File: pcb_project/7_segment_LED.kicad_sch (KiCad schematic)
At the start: 1 part, among them U5 MAX7221xWG

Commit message: LED & FPGA_Started
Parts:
- added C24: 10µF electrolytic, symbol Device:C
- added C25: 0.1µF ceramic, symbol Device:C
- added R40: 18KOhm, symbol Device:R
- added U6: COM-11405, COM-11405_SPK, symbol 11405_ATA8041:COM-11405
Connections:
- net LED_MOSI: now reaches U5.1 (DIN)
- net at U5.11 (DIG_1): now also U6.9 (DIG2)
- net LED_CS: now reaches U5.12 (~{CS})
- net LED_CLK: now reaches U5.13 (CLK)
- net SEGA (11): now reaches U5.14 (SEG_A)
- net SEGA (11): now also U6.11 (A)
- net SEGF (10): now reaches U5.15 (SEG_F)
- net SEGF (10): now also U6.10 (F)
- net SEGB (7): now reaches U5.16 (SEG_B)
- net SEGB (7): now also U6.7 (B)
- net SEGG (5): now reaches U5.17 (SEG_G)
- net SEGG (5): now also U6.5 (G)
- net at U5.18 (ISET): now also R40.2
- net +5V: now reaches U5.19 (V+)
- net +5V: now also C24.1, C25.1, R40.1
- net at U5.2 (DIG_0): now also U6.12 (Dig1)
- net SEGC (4): now reaches U5.20 (SEG_C)
- net SEGC (4): now also U6.4 (C)
- net SEGE (1): now reaches U5.21 (SEG_E)
- net SEGE (1): now also U6.1 (E)
- net at U5.22 (SEG_DP): now also U6.3 (DP)
- net SEGD(2): now reaches U5.23 (SEG_D)
- net SEGD(2): now also U6.2 (D)
- net LED_MISO: now reaches U5.24 (DOUT)
- net GND: now reaches U5.4 (GND), U5.9 (GND)
- net GND: now also C24.2, C25.2
- net at U5.6 (DIG_2): now also U6.8 (DIG3)
- net at U5.7 (DIG_3): now also U6.6 (DIG4)
- no-connect marks 0 -> 4

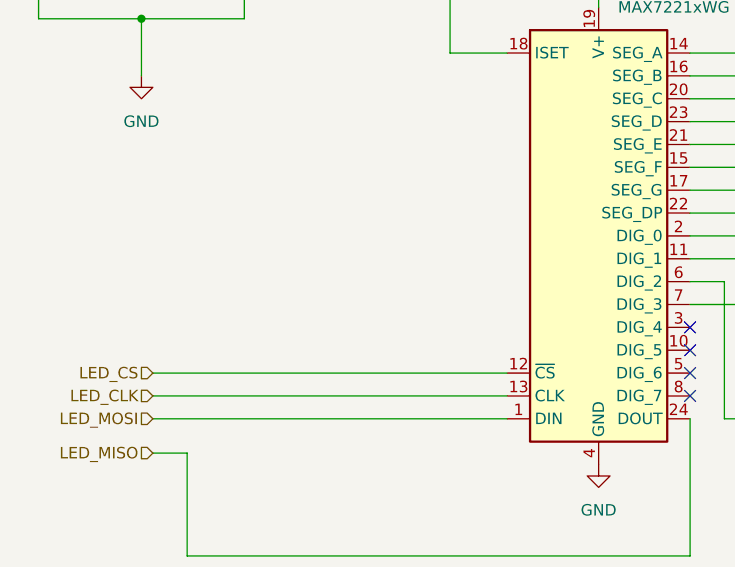
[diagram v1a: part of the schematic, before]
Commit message: Connect Controller, LED-display, USB and SD reader to MCU
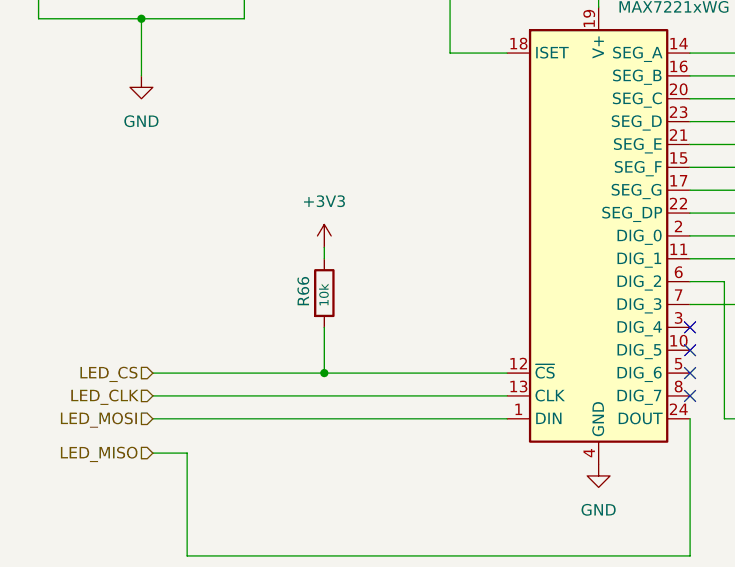
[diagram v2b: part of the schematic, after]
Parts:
- added R66: 10k, symbol Device:R
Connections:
- net LED_CS: now also R66.2
- new net +3V3: R66.1
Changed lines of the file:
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@@
 	(paper "A4")
+	(junction
+		(at 78.74 102.87)
+		(diameter 0)
+		(color 0 0 0 0)
+	)
 	(junction
 		(at 109.22 41.91)
@@
 	(wire
 		(pts
+			(xy 78.74 97.79) (xy 78.74 102.87)
+		)
+		(stroke
+			(width 0)
+			(type default)
+		)
+	)
+	(wire
+		(pts
+			(xy 78.74 102.87) (xy 99.06 102.87)
+		)
+		(stroke
+			(width 0)
+			(type default)
+		)
+	)
+	(wire
+		(pts
 			(xy 119.38 85.09) (xy 128.27 85.09)
 		)
@@
 	(wire
 		(pts
-			(xy 59.69 102.87) (xy 99.06 102.87)
+			(xy 59.69 102.87) (xy 78.74 102.87)
 		)
 		(stroke
@@
 		(pts
 			(xy 146.05 72.39) (xy 146.05 82.55)
+		)
+		(stroke
+			(width 0)
+			(type default)
+		)
+	)
+	(wire
+		(pts
+			(xy 78.74 90.17) (xy 78.74 88.9)
 		)
 		(stroke
@@
 	)
 	(symbol
+		(lib_id "power:+3V3")
+		(at 78.74 88.9 0)
+		(unit 1)
+		(exclude_from_sim no)
+		(in_bom yes)
+		(on_board yes)
+		(dnp no)
+		(fields_autoplaced yes)
+		(property "Reference" "#PWR056"
+			(at 78.74 92.71 0)
+			(effects
+				(font
+					(size 1.27 1.27)
+				)
+				(hide yes)
+			)
+		)
+		(property "Value" "+3V3"
+			(at 78.74 83.82 0)
+			(effects
+				(font
+					(size 1.27 1.27)
+				)
+			)
+		)
+		(property "Footprint" ""
+			(at 78.74 88.9 0)
+			(effects
+				(font
+					(size 1.27 1.27)
+				)
+				(hide yes)
+			)
+		)
+		(property "Datasheet" ""
+			(at 78.74 88.9 0)
+			(effects
+				(font
+					(size 1.27 1.27)
+				)
+				(hide yes)
+			)
+		)
+		(property "Description" "Power symbol creates a global label with name \"+3V3\""
+			(at 78.74 88.9 0)
+			(effects
+				(font
+					(size 1.27 1.27)
+				)
+				(hide yes)
+			)
+		)
+		(pin "1"
+		)
+		(instances
+			(project ""
+				(path "/98f80f66-4595-4d0f-90ca-59b2db6f447b/35305def-b224-49b9-b18d-edcf9292ca07"
+					(reference "#PWR056")
+					(unit 1)
+				)
+			)
+		)
+	)
+	(symbol
 		(lib_id "power:GND")
 		(at 109.22 113.03 0)
@@
 					(unit 1)
 				)
+			)
+		)
+	)
+	(symbol
+		(lib_id "Device:R")
+		(at 78.74 93.98 0)
+		(unit 1)
+		(exclude_from_sim no)
+		(in_bom yes)
+		(on_board yes)
+		(dnp no)
+		(property "Reference" "R66"
+			(at 76.454 95.504 90)
+			(effects
+				(font
+					(size 1.27 1.27)
+				)
+				(justify left)
+			)
+		)
+		(property "Value" "10k"
+			(at 78.74 95.504 90)
+			(effects
+				(font
+					(size 1.016 1.016)
+				)
+				(justify left)
+			)
+		)
+		(property "Footprint" ""
+			(at 76.962 93.98 90)
+			(effects
+				(font
+					(size 1.27 1.27)
+				)
+				(hide yes)
+			)
+		)
+		(property "Datasheet" "~"
+			(at 78.74 93.98 0)
+			(effects
+				(font
+					(size 1.27 1.27)
+				)
+				(hide yes)
+			)
+		)
+		(property "Description" "Resistor"
+			(at 78.74 93.98 0)
+			(effects
+				(font
+					(size 1.27 1.27)
+				)
+				(hide yes)
+			)
+		)
+		(pin "1"
+		)
+		(pin "2"
+		)
+		(instances
+			(project ""
+				(path "/98f80f66-4595-4d0f-90ca-59b2db6f447b/35305def-b224-49b9-b18d-edcf9292ca07"
+					(reference "R66")
+					(unit 1)
+				)

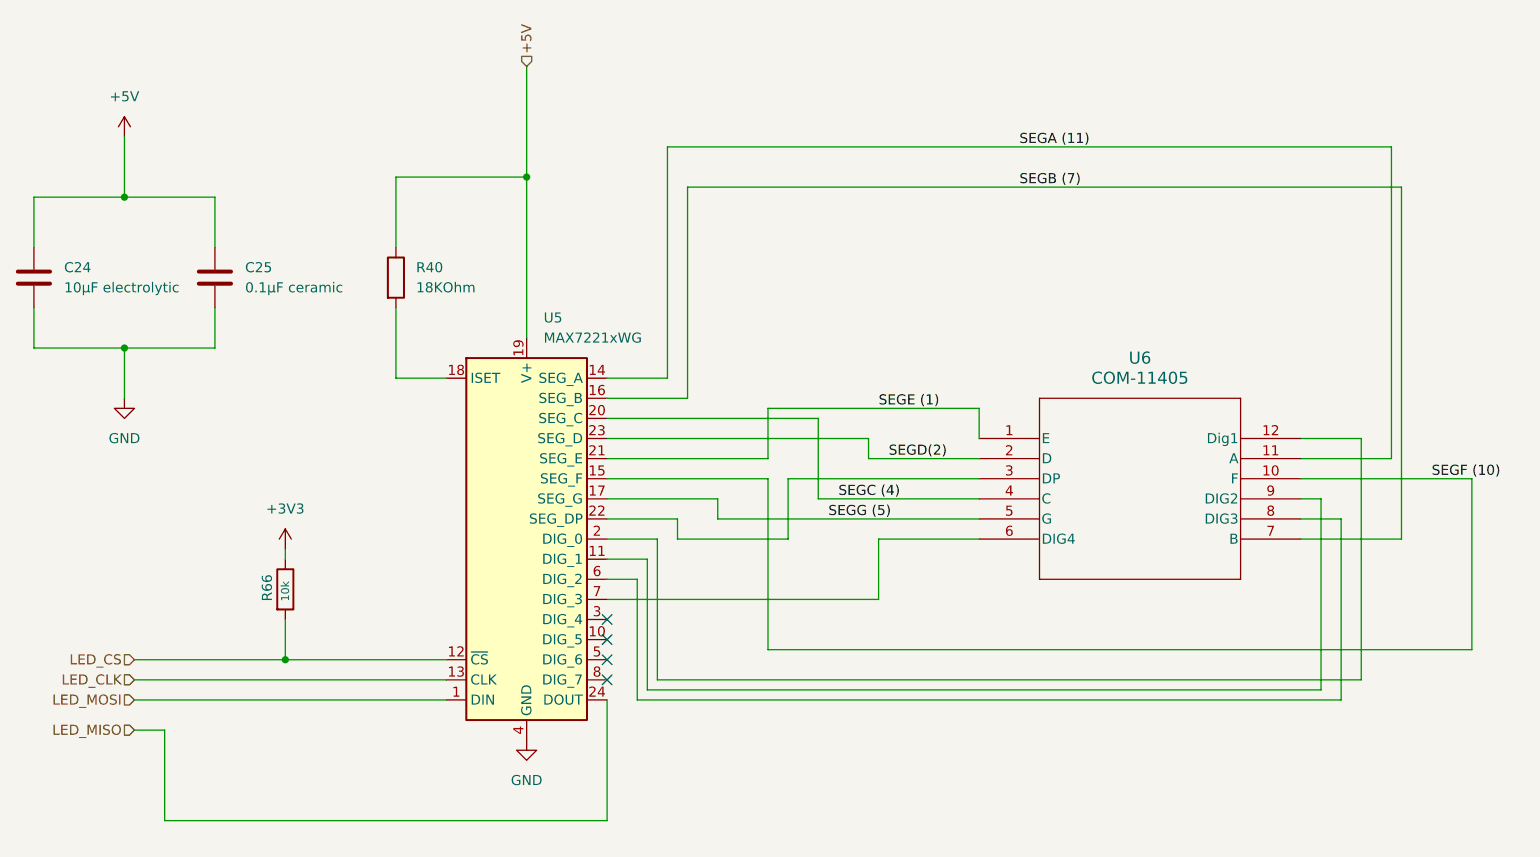
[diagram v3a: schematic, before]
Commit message: ERC fixes, some remain
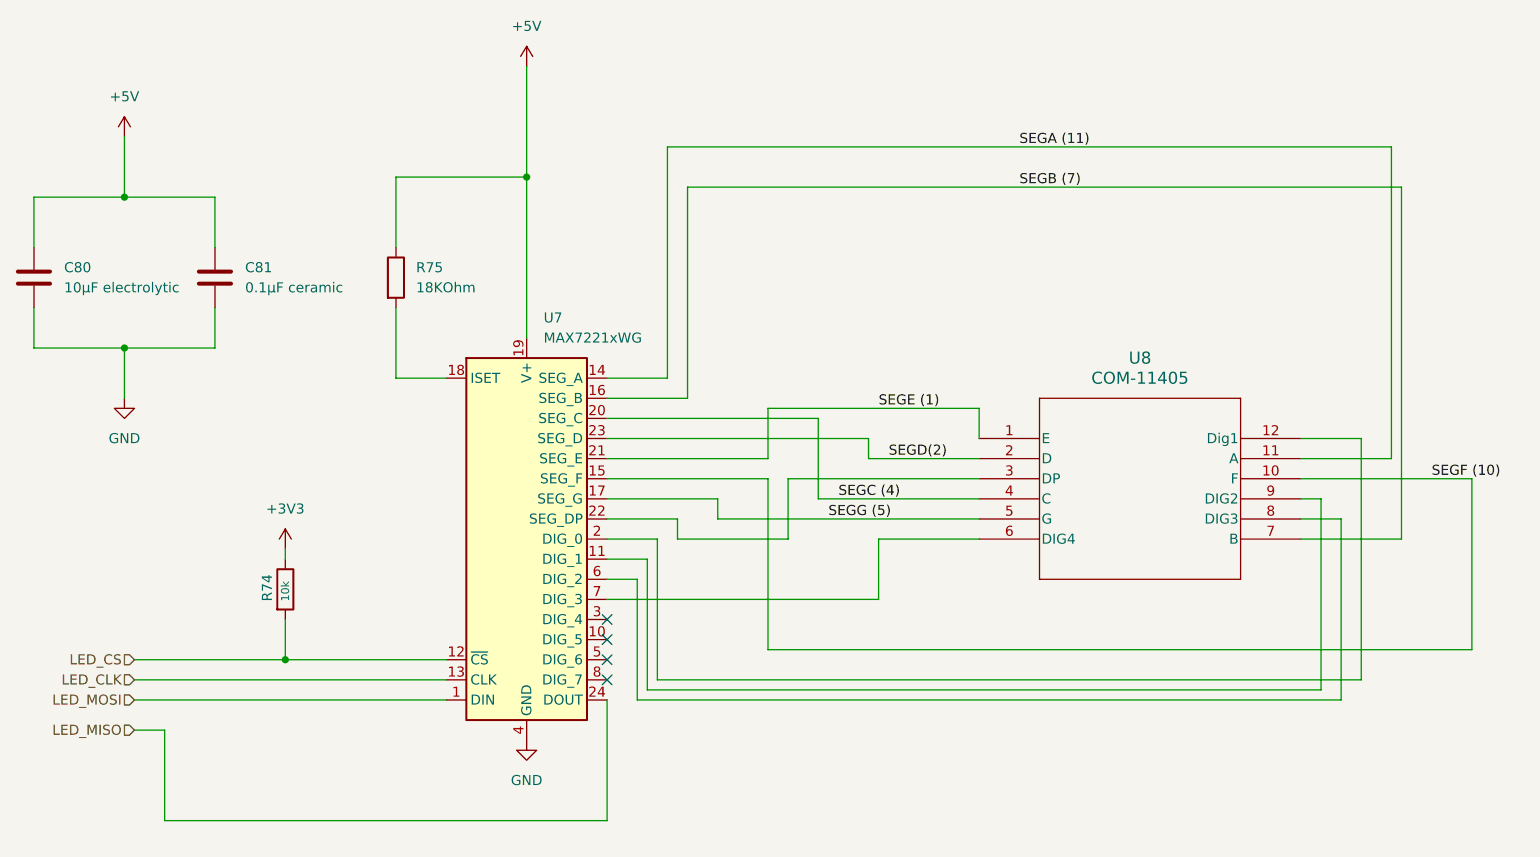
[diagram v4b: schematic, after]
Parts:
- renumbered C24 to C80, C25 to C81, R66 to R74, R40 to R75, U5 to U7, U6 to U8
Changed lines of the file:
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@@
-		)
-	)
-	(hierarchical_label "+5V"
-		(shape input)
-		(at 109.22 27.94 90)
-		(effects
-			(font
-				(size 1.27 1.27)
-			)
-			(justify left)
 		)
 	)
@@
 		(dnp no)
 		(fields_autoplaced yes)
-		(property "Reference" "U5"
+		(property "Reference" "U7"
 			(at 111.3633 59.69 0)
 			(effects
@@
 			(project ""
 				(path "/98f80f66-4595-4d0f-90ca-59b2db6f447b/35305def-b224-49b9-b18d-edcf9292ca07"
-					(reference "U5")
+					(reference "U7")
 					(unit 1)
 				)
@@
 		(dnp no)
 		(fields_autoplaced yes)
-		(property "Reference" "#PWR0111"
+		(property "Reference" "#PWR099"
 			(at 78.74 92.71 0)
 			(effects
@@
 			(project ""
 				(path "/98f80f66-4595-4d0f-90ca-59b2db6f447b/35305def-b224-49b9-b18d-edcf9292ca07"
-					(reference "#PWR0111")
+					(reference "#PWR099")
 					(unit 1)
 				)
@@
 		(dnp no)
 		(fields_autoplaced yes)
-		(property "Reference" "#PWR0113"
+		(property "Reference" "#PWR0101"
 			(at 109.22 119.38 0)
 			(effects
@@
 			(project ""
 				(path "/98f80f66-4595-4d0f-90ca-59b2db6f447b/35305def-b224-49b9-b18d-edcf9292ca07"
-					(reference "#PWR0113")
+					(reference "#PWR0101")
 					(unit 1)
 				)
@@
 		(dnp no)
 		(fields_autoplaced yes)
-		(property "Reference" "R40"
+		(property "Reference" "R75"
 			(at 95.25 53.3399 0)
 			(effects
@@
 			(project ""
 				(path "/98f80f66-4595-4d0f-90ca-59b2db6f447b/35305def-b224-49b9-b18d-edcf9292ca07"
-					(reference "R40")
+					(reference "R75")
 					(unit 1)
 				)
@@
 		(on_board yes)
 		(dnp no)
-		(property "Reference" "R66"
+		(property "Reference" "R74"
 			(at 76.454 95.504 90)
 			(effects
@@
 			(project ""
 				(path "/98f80f66-4595-4d0f-90ca-59b2db6f447b/35305def-b224-49b9-b18d-edcf9292ca07"
-					(reference "R66")
+					(reference "R74")
 					(unit 1)
 				)
@@
 		(dnp no)
 		(fields_autoplaced yes)
-		(property "Reference" "C24"
+		(property "Reference" "C80"
 			(at 50.8 53.3399 0)
 			(effects
@@
 			(project ""
 				(path "/98f80f66-4595-4d0f-90ca-59b2db6f447b/35305def-b224-49b9-b18d-edcf9292ca07"
-					(reference "C24")
+					(reference "C80")
 					(unit 1)
 				)
@@
 		(dnp no)
 		(fields_autoplaced yes)
-		(property "Reference" "#PWR0112"
+		(property "Reference" "#PWR098"
 			(at 58.42 76.2 0)
 			(effects
@@
 			(project ""
 				(path "/98f80f66-4595-4d0f-90ca-59b2db6f447b/35305def-b224-49b9-b18d-edcf9292ca07"
-					(reference "#PWR0112")
+					(reference "#PWR098")
 					(unit 1)
 				)
@@
 		(dnp no)
 		(fields_autoplaced yes)
-		(property "Reference" "U6"
+		(property "Reference" "U8"
 			(at 186.69 64.77 0)
 			(effects
@@
 			(project ""
 				(path "/98f80f66-4595-4d0f-90ca-59b2db6f447b/35305def-b224-49b9-b18d-edcf9292ca07"
-					(reference "U6")
+					(reference "U8")
 					(unit 1)
 				)
@@
 		(dnp no)
 		(fields_autoplaced yes)
-		(property "Reference" "#PWR0114"
+		(property "Reference" "#PWR097"
 			(at 58.42 40.64 0)
 			(effects
@@
 			(project ""
 				(path "/98f80f66-4595-4d0f-90ca-59b2db6f447b/35305def-b224-49b9-b18d-edcf9292ca07"
-					(reference "#PWR0114")
+					(reference "#PWR097")
 					(unit 1)
 				)
@@
 		(dnp no)
 		(fields_autoplaced yes)
-		(property "Reference" "C25"
+		(property "Reference" "C81"
 			(at 73.66 53.3399 0)
 			(effects
@@
 			(project ""
 				(path "/98f80f66-4595-4d0f-90ca-59b2db6f447b/35305def-b224-49b9-b18d-edcf9292ca07"
-					(reference "C25")
-					(unit 1)
-				)
+					(reference "C81")
+					(unit 1)
+				)
+			)
+		)
+	)
+	(symbol
+		(lib_id "power:+5V")
+		(at 109.22 27.94 0)
+		(unit 1)
+		(exclude_from_sim no)
+		(in_bom yes)
+		(on_board yes)
+		(dnp no)
+		(fields_autoplaced yes)
+		(property "Reference" "#PWR0100"
+			(at 109.22 31.75 0)
+			(effects
+				(font
+					(size 1.27 1.27)
+				)
+				(hide yes)
+			)
+		)
+		(property "Value" "+5V"
+			(at 109.22 22.86 0)
+			(effects
+				(font
+					(size 1.27 1.27)
+				)
+			)
+		)
+		(property "Footprint" ""
+			(at 109.22 27.94 0)
+			(effects
+				(font
+					(size 1.27 1.27)
+				)
+				(hide yes)
+			)
+		)
+		(property "Datasheet" ""
+			(at 109.22 27.94 0)
+			(effects
+				(font
+					(size 1.27 1.27)
+				)
+				(hide yes)
+			)
+		)
+		(property "Description" "Power symbol creates a global label with name \"+5V\""
+			(at 109.22 27.94 0)
+			(effects
+				(font
+					(size 1.27 1.27)
+				)
+				(hide yes)
+			)
+		)
+		(pin "1"
+		)
+		(instances
+			(project ""
+				(path "/98f80f66-4595-4d0f-90ca-59b2db6f447b/35305def-b224-49b9-b18d-edcf9292ca07"
+					(reference "#PWR0100")
+					(unit 1)
+				)

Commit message: Fix JTAG connector, add pullups (FPGA has internal pullups as well), add some capacitor footprints
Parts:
- U8: footprint COM-11405_SPK -> Project_Footprints:COM-11405_SPK
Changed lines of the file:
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@@
 			)
 		)
-		(property "Footprint" "COM-11405_SPK"
+		(property "Footprint" "Project_Footprints:COM-11405_SPK"
 			(at 166.37 74.93 0)
 			(effects

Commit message: Add most footprints, missing some inductors and 3 buttons
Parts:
- C80: footprint (none) -> Capacitor_THT:CP_Radial_D5.0mm_P2.00mm
- C81: footprint (none) -> Capacitor_SMD:C_0603_1608Metric_Pad1.08x0.95mm_HandSolder
- R74, R75: footprint (none) -> Resistor_SMD:R_0805_2012Metric_Pad1.20x1.40mm_HandSolder
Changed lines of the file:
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@@
 			)
 		)
-		(property "Footprint" ""
+		(property "Footprint" "Resistor_SMD:R_0805_2012Metric_Pad1.20x1.40mm_HandSolder"
 			(at 90.932 54.61 90)
 			(effects
@@
 			)
 		)
-		(property "Footprint" ""
+		(property "Footprint" "Resistor_SMD:R_0805_2012Metric_Pad1.20x1.40mm_HandSolder"
 			(at 76.962 93.98 90)
 			(effects
@@
 			)
 		)
-		(property "Footprint" ""
+		(property "Footprint" "Capacitor_THT:CP_Radial_D5.0mm_P2.00mm"
 			(at 47.9552 58.42 0)
 			(effects
@@
 			)
 		)
-		(property "Footprint" ""
+		(property "Footprint" "Capacitor_SMD:C_0603_1608Metric_Pad1.08x0.95mm_HandSolder"
 			(at 70.8152 58.42 0)
 			(effects
